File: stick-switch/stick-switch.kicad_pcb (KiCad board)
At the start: 2 copper layers, 30 x 30 mm, 4 parts, among them J1 Conn_01x04

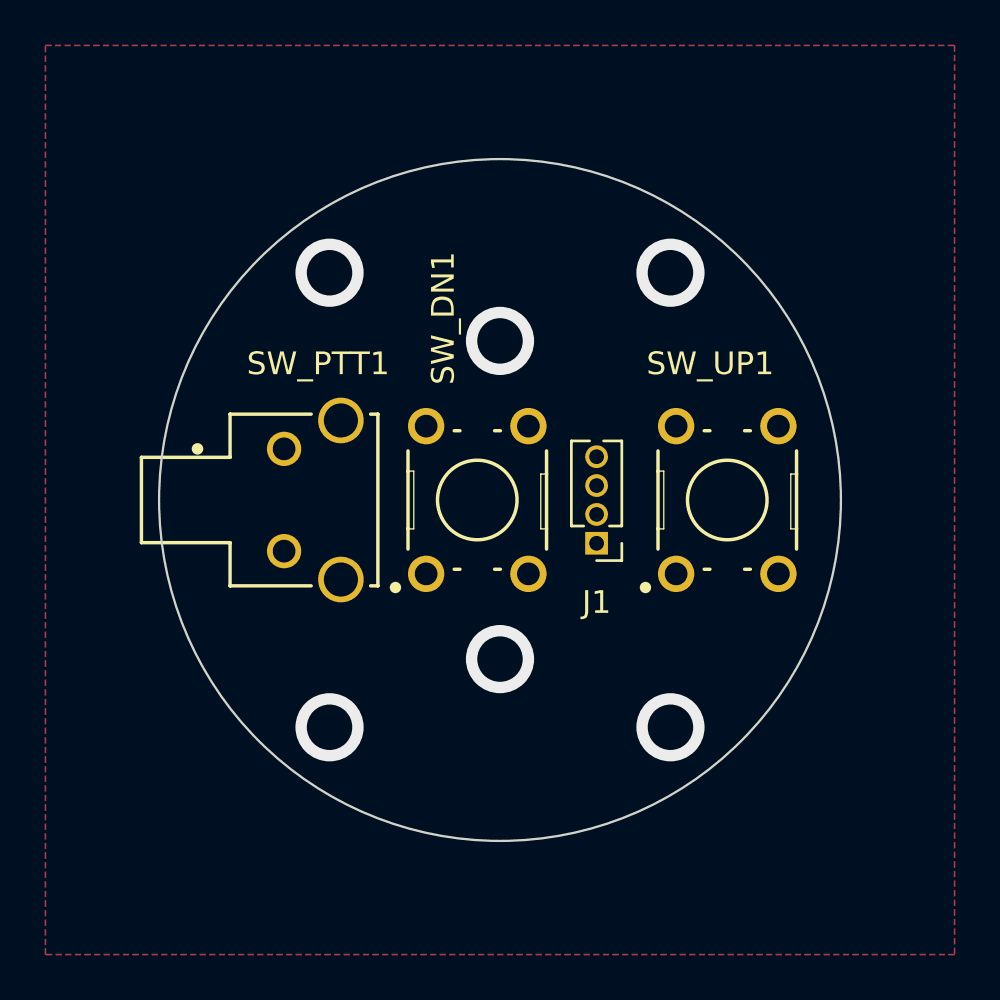
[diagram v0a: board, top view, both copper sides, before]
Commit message: Use real mounting holes, not just vias.
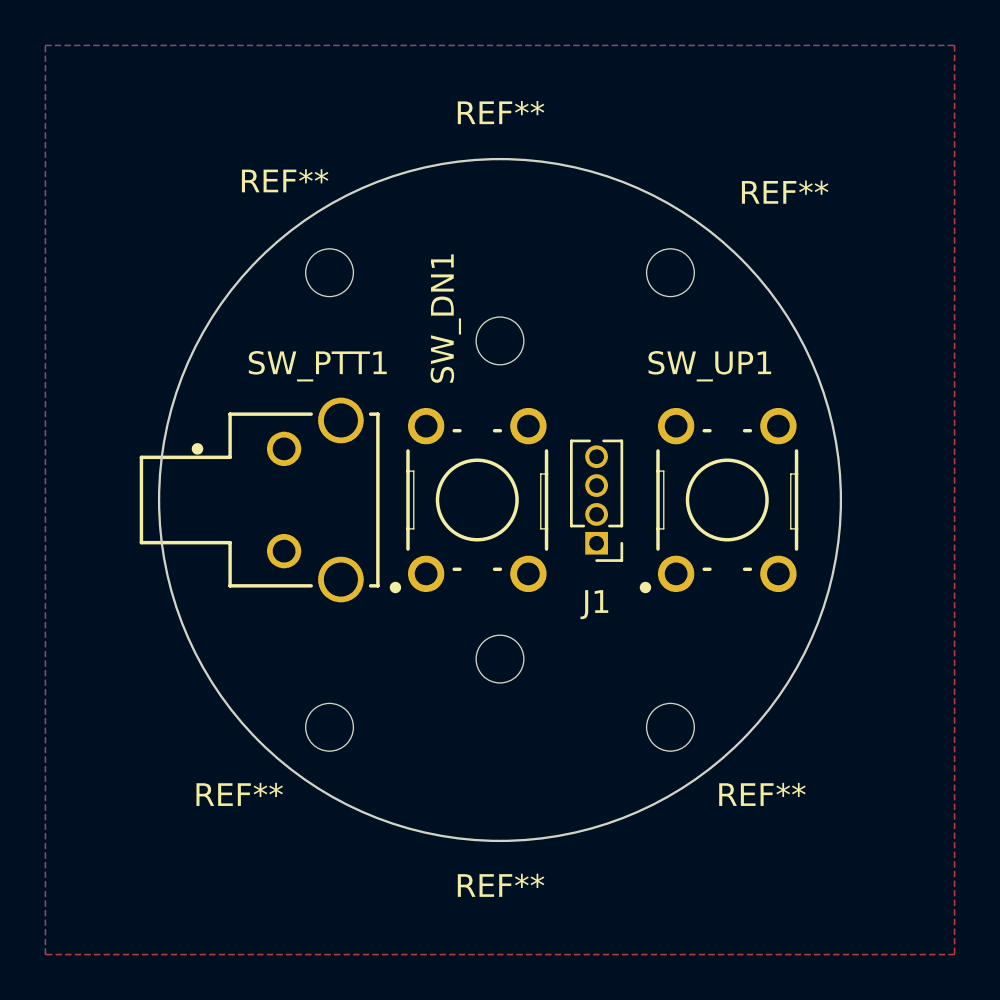
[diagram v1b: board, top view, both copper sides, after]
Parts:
- added REF**: MountingHole_2.1mm, MountingHole:MountingHole_2.1mm, F.Cu at (7.50, 10.0)
- added REF**: MountingHole_2.1mm, MountingHole:MountingHole_2.1mm, F.Cu at (7.50, -10.0)
- added REF**: MountingHole_2.1mm, MountingHole:MountingHole_2.1mm, F.Cu at (0.00, 7.00)
- added REF**: MountingHole_2.1mm, MountingHole:MountingHole_2.1mm, F.Cu at (-7.50, -10.0)
- added REF**: MountingHole_2.1mm, MountingHole:MountingHole_2.1mm, F.Cu at (0.00, -7.00)
- added REF**: MountingHole_2.1mm, MountingHole:MountingHole_2.1mm, F.Cu at (-7.50, 10.0)
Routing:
- net /COM: vias 6 -> 0
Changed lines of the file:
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@@
     )
+  )
+  (footprint "MountingHole:MountingHole_2.1mm" (layer "F.Cu")
+    (at 7.5 10)
+    (descr "Mounting Hole 2.1mm, no annular")
+    (tags "mounting hole 2.1mm no annular")
+    (attr exclude_from_pos_files exclude_from_bom)
+    (fp_text reference "REF**" (at 4 3) (layer "F.SilkS")
+      (effects (font (size 1 1) (thickness 0.15)))
+    )
+    (fp_text value "MountingHole_2.1mm" (at 0 3.2) (layer "F.Fab")
+      (effects (font (size 1 1) (thickness 0.15)))
+    )
+    (fp_text user "${REFERENCE}" (at 0 0) (layer "F.Fab")
+      (effects (font (size 1 1) (thickness 0.15)))
+    )
+    (fp_circle (center 0 0) (end 2.1 0) (layer "Cmts.User") (width 0.15) (fill none))
+    (fp_circle (center 0 0) (end 2.35 0) (layer "F.CrtYd") (width 0.05) (fill none))
+    (pad "" np_thru_hole circle (at 0 0) (size 2.1 2.1) (drill 2.1) (layers *.Cu *.Mask))
+  )
+  (footprint "MountingHole:MountingHole_2.1mm" (layer "F.Cu")
+    (at 7.5 -10)
+    (descr "Mounting Hole 2.1mm, no annular")
+    (tags "mounting hole 2.1mm no annular")
+    (attr exclude_from_pos_files exclude_from_bom)
+    (fp_text reference "REF**" (at 5 -3.5) (layer "F.SilkS")
+      (effects (font (size 1 1) (thickness 0.15)))
+    )
+    (fp_text value "MountingHole_2.1mm" (at 0 3.2) (layer "F.Fab")
+      (effects (font (size 1 1) (thickness 0.15)))
+    )
+    (fp_text user "${REFERENCE}" (at 0 0) (layer "F.Fab")
+      (effects (font (size 1 1) (thickness 0.15)))
+    )
+    (fp_circle (center 0 0) (end 2.1 0) (layer "Cmts.User") (width 0.15) (fill none))
+    (fp_circle (center 0 0) (end 2.35 0) (layer "F.CrtYd") (width 0.05) (fill none))
+    (pad "" np_thru_hole circle (at 0 0) (size 2.1 2.1) (drill 2.1) (layers *.Cu *.Mask))
+  )
+  (footprint "MountingHole:MountingHole_2.1mm" (layer "F.Cu")
+    (at 0 7)
+    (descr "Mounting Hole 2.1mm, no annular")
+    (tags "mounting hole 2.1mm no annular")
+    (attr exclude_from_pos_files exclude_from_bom)
+    (fp_text reference "REF**" (at 0 10) (layer "F.SilkS")
+      (effects (font (size 1 1) (thickness 0.15)))
+    )
+    (fp_text value "MountingHole_2.1mm" (at 0 3.2) (layer "F.Fab")
+      (effects (font (size 1 1) (thickness 0.15)))
+    )
+    (fp_text user "${REFERENCE}" (at 0 0) (layer "F.Fab")
+      (effects (font (size 1 1) (thickness 0.15)))
+    )
+    (fp_circle (center 0 0) (end 2.1 0) (layer "Cmts.User") (width 0.15) (fill none))
+    (fp_circle (center 0 0) (end 2.35 0) (layer "F.CrtYd") (width 0.05) (fill none))
+    (pad "" np_thru_hole circle (at 0 0) (size 2.1 2.1) (drill 2.1) (layers *.Cu *.Mask))
+  )
+  (footprint "MountingHole:MountingHole_2.1mm" (layer "F.Cu")
+    (at -7.5 -10)
+    (descr "Mounting Hole 2.1mm, no annular")
+    (tags "mounting hole 2.1mm no annular")
+    (attr exclude_from_pos_files exclude_from_bom)
+    (fp_text reference "REF**" (at -2 -4) (layer "F.SilkS")
+      (effects (font (size 1 1) (thickness 0.15)))
+    )
+    (fp_text value "MountingHole_2.1mm" (at 0 3.2) (layer "F.Fab")
+      (effects (font (size 1 1) (thickness 0.15)))
+    )
+    (fp_text user "${REFERENCE}" (at 0 0) (layer "F.Fab")
+      (effects (font (size 1 1) (thickness 0.15)))
+    )
+    (fp_circle (center 0 0) (end 2.1 0) (layer "Cmts.User") (width 0.15) (fill none))
+    (fp_circle (center 0 0) (end 2.35 0) (layer "F.CrtYd") (width 0.05) (fill none))
+    (pad "" np_thru_hole circle (at 0 0) (size 2.1 2.1) (drill 2.1) (layers *.Cu *.Mask))
+  )
+  (footprint "MountingHole:MountingHole_2.1mm" (layer "F.Cu")
+    (at 0 -7)
+    (descr "Mounting Hole 2.1mm, no annular")
+    (tags "mounting hole 2.1mm no annular")
+    (attr exclude_from_pos_files exclude_from_bom)
+    (fp_text reference "REF**" (at 0 -10) (layer "F.SilkS")
+      (effects (font (size 1 1) (thickness 0.15)))
+    )
+    (fp_text value "MountingHole_2.1mm" (at 0 3.2) (layer "F.Fab")
+      (effects (font (size 1 1) (thickness 0.15)))
+    )
+    (fp_text user "${REFERENCE}" (at 0 0) (layer "F.Fab")
+      (effects (font (size 1 1) (thickness 0.15)))
+    )
+    (fp_circle (center 0 0) (end 2.1 0) (layer "Cmts.User") (width 0.15) (fill none))
+    (fp_circle (center 0 0) (end 2.35 0) (layer "F.CrtYd") (width 0.05) (fill none))
+    (pad "" np_thru_hole circle (at 0 0) (size 2.1 2.1) (drill 2.1) (layers *.Cu *.Mask))
   )
   (footprint "Connector_PinHeader_1.27mm:PinHeader_1x04_P1.27mm_Vertical" (layer "F.Cu")
@@
     )
   )
+  (footprint "MountingHole:MountingHole_2.1mm" (layer "F.Cu")
+    (at -7.5 10)
+    (descr "Mounting Hole 2.1mm, no annular")
+    (tags "mounting hole 2.1mm no annular")
+    (attr exclude_from_pos_files exclude_from_bom)
+    (fp_text reference "REF**" (at -4 3) (layer "F.SilkS")
+      (effects (font (size 1 1) (thickness 0.15)))
+    )
+    (fp_text value "MountingHole_2.1mm" (at 0 3.2) (layer "F.Fab")
+      (effects (font (size 1 1) (thickness 0.15)))
+    )
+    (fp_text user "${REFERENCE}" (at 0 0) (layer "F.Fab")
+      (effects (font (size 1 1) (thickness 0.15)))
+    )
+    (fp_circle (center 0 0) (end 2.1 0) (layer "Cmts.User") (width 0.15) (fill none))
+    (fp_circle (center 0 0) (end 2.35 0) (layer "F.CrtYd") (width 0.05) (fill none))
+    (pad "" np_thru_hole circle (at 0 0) (size 2.1 2.1) (drill 2.1) (layers *.Cu *.Mask))
+  )
   (gr_circle (center 0 0) (end 0 9.525) (layer "B.SilkS") (width 0.15) (fill none))
   (gr_circle (center 0 0) (end 0 15) (layer "Edge.Cuts") (width 0.1) (fill none))
-  (via (at -7.5 -10) (size 3) (drill 2) (layers "F.Cu" "B.Cu") (free) (net 4))
-  (via (at 7.5 10) (size 3) (drill 2) (layers "F.Cu" "B.Cu") (free) (net 4))
-  (via (at 7.5 -10) (size 3) (drill 2) (layers "F.Cu" "B.Cu") (free) (net 4))
-  (via (at 0 -7) (size 3) (drill 2) (layers "F.Cu" "B.Cu") (free) (net 4))
-  (via (at -7.5 10) (size 3) (drill 2) (layers "F.Cu" "B.Cu") (free) (net 4))
-  (via (at 0 7) (size 3) (drill 2) (layers "F.Cu" "B.Cu") (free) (net 4))
   (zone (net 4) (net_name "/COM") (layers F&B.Cu) (hatch edge 0.508)
     (connect_pads (clearance 0.2))

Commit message: Moved mounting holes.
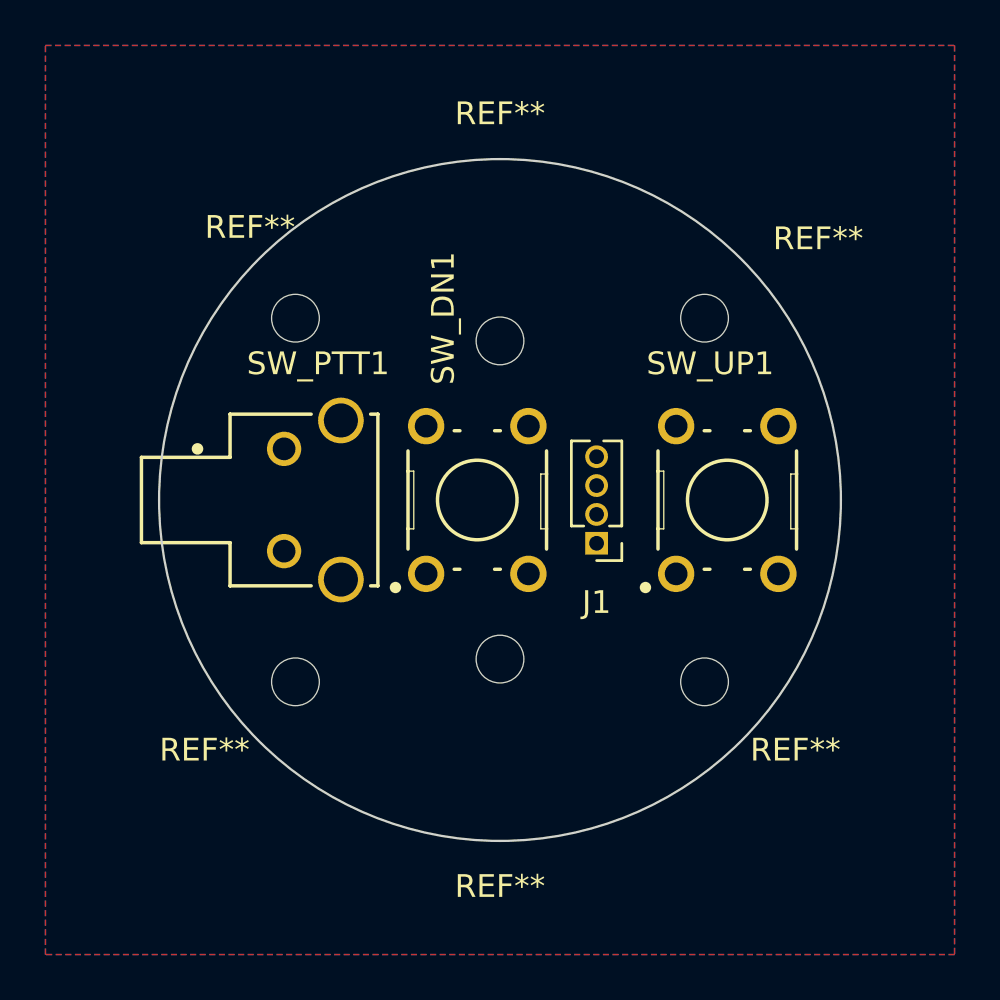
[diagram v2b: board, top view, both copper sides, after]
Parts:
- moved REF** 2.50 mm to (9.00, 8.00)
- moved REF** 2.50 mm to (9.00, -8.00)
- moved REF** 2.50 mm to (-9.00, -8.00)
- moved REF** 2.50 mm to (-9.00, 8.00)
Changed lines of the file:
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@@
   )
   (footprint "MountingHole:MountingHole_2.1mm" (layer "F.Cu")
-    (at 7.5 10)
+    (at 9 8)
     (descr "Mounting Hole 2.1mm, no annular")
     (tags "mounting hole 2.1mm no annular")
@@
   )
   (footprint "MountingHole:MountingHole_2.1mm" (layer "F.Cu")
-    (at 7.5 -10)
+    (at 9 -8)
     (descr "Mounting Hole 2.1mm, no annular")
     (tags "mounting hole 2.1mm no annular")
@@
   )
   (footprint "MountingHole:MountingHole_2.1mm" (layer "F.Cu")
-    (at -7.5 -10)
+    (at -9 -8)
     (descr "Mounting Hole 2.1mm, no annular")
     (tags "mounting hole 2.1mm no annular")
@@
     (fp_circle (center 0 0) (end 2.1 0) (layer "Cmts.User") (width 0.15) (fill none))
     (fp_circle (center 0 0) (end 2.35 0) (layer "F.CrtYd") (width 0.05) (fill none))
-    (pad "" np_thru_hole circle (at 0 0) (size 2.1 2.1) (drill 2.1) (layers *.Cu *.Mask))
+    (pad "" np_thru_hole circle (at 0 0) (size 2.1 2.1) (drill 2.1) (layers F&B.Cu *.Mask))
   )
   (footprint "MountingHole:MountingHole_2.1mm" (layer "F.Cu")
@@
   )
   (footprint "MountingHole:MountingHole_2.1mm" (layer "F.Cu")
-    (at -7.5 10)
-    (descr "Mounting Hole 2.1mm, no annular")
-    (tags "mounting hole 2.1mm no annular")
+    (at -9 8)
+    (descr "Mounting Hole 2.1mm, no annular")
+    (tags "mounting hole 2.1mm no annular")

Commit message: Made PTT and Trim common separate nets. Finalized layout and generated Gerbers.
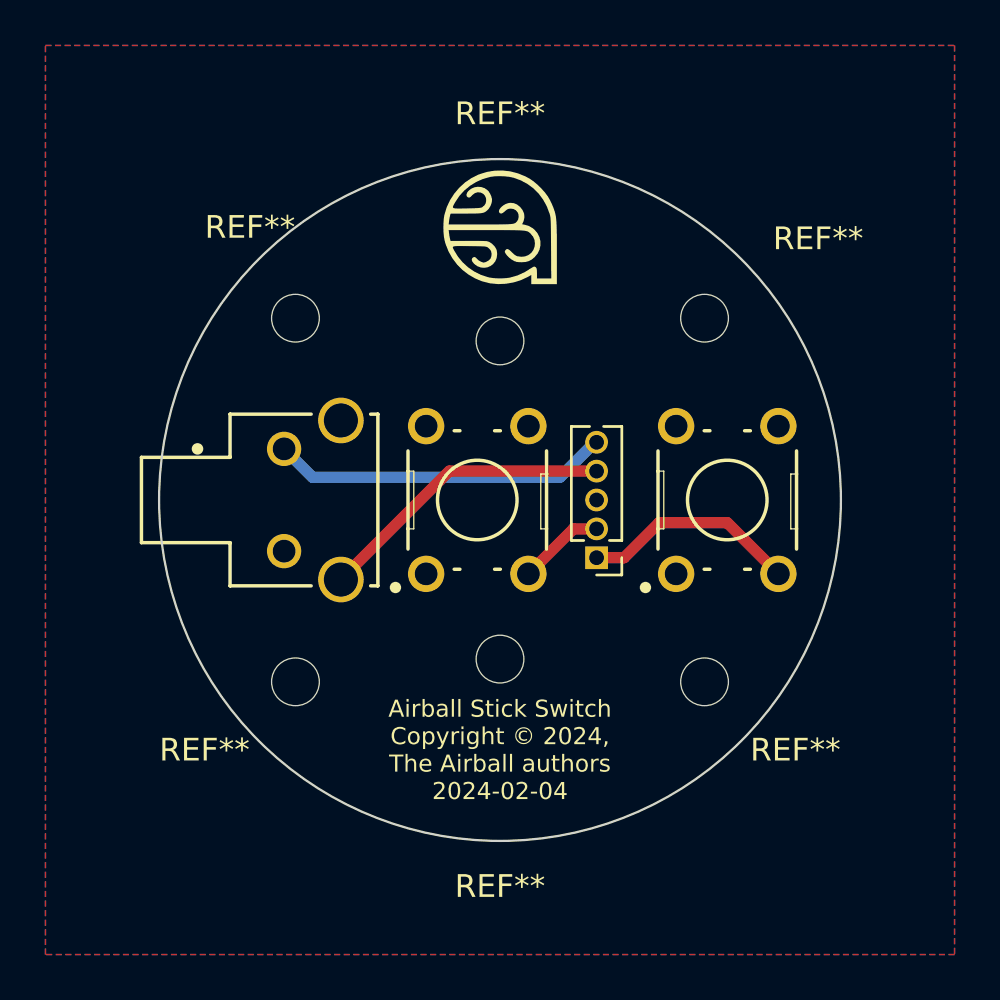
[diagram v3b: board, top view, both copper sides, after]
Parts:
- added G***: LOGO, airball-hardware:airball-logo-5mm, F.Cu at (0.00, -12.0)
- J1: footprint Connector_PinHeader_1.27mm:PinHeader_1x04_P1.27mm_Vertical -> Connector_PinHeader_1.27mm:PinHeader_1x05_P1.27mm_Vertical
- moved J1 0.64 mm to (4.25, 2.54)
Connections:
- J1 pad 3: /PTT -> /TRIM_COM
- J1 pad 4: /COM -> /PTT
- SW_DN1 pad 2: /COM -> /TRIM_COM
- SW_PTT1 pad 1: unconnected-(SW_PTT1-Pad1) -> /PTT_COM
- SW_PTT1 pad 2: /PTT -> unconnected-(SW_PTT1-Pad2)
- SW_PTT1 pad 3: /COM -> unconnected-(SW_PTT1-Pad3)
- SW_PTT1 pad 4: unconnected-(SW_PTT1-Pad4) -> /PTT
- SW_UP1 pad 2: /COM -> /TRIM_COM
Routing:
- net /PTT_COM: track 0.00 -> 14.9 mm
- net /PTT: track 0.00 -> 13.2 mm
- net /UP: track 0.00 -> 9.57 mm
- net /DN: track 0.00 -> 3.82 mm
- added copper zone on B.Cu, net /TRIM_COM
- added copper zone on F.Cu, net /TRIM_COM
- removed copper zone on B.Cu, net /COM
- removed copper zone on F.Cu, net /COM
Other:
- board text added: "Airball Stick Switch Copyright © 2024, The Airball authors 2024-02-04"
